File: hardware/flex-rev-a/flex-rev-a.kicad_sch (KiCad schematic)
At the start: 0 parts

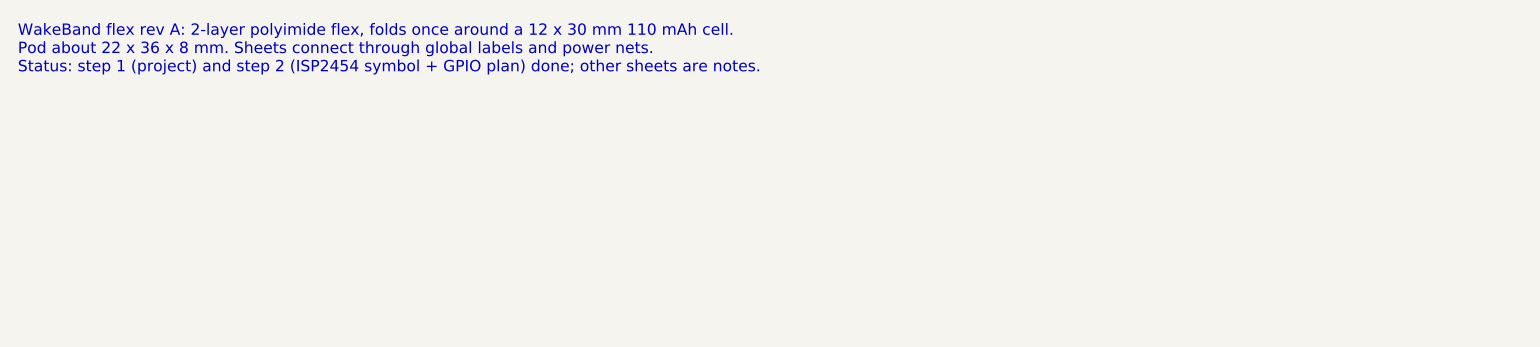
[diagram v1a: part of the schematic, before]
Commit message: Draw nPM1304 power sheet and move the project to KiCad 10 format
Power sheet (step 3 of the flex plan), from Nordic's nPM1304 datasheet
reference circuit "configuration 2" (QFN32):
- VBUS from dock VIN with a TVS and 1 uF; CC1/CC2 to GND (no USB-C).
- VBAT to the cell pads through a cut-able current-measure jumper (JP201).
- BUCK1 at 1.8 V (VSET1 47k, confirmed in the datasheet table) on VDD_1V8,
  2.2 uH + 10 uF; VDDIO from VOUT1; PVSS1 to GND through a net tie.
- BUCK2 unused: VOUT2 to VSYS, VSET2 and PVSS2 to GND, SW2 open, no inductor.
  Load switches unused (pins to GND), LED pins open.
- 10k B3380 NTC, SHPHLD test pad + DNP pull-up and button footprint,
  PMIC_INT on GPIO3, 4.7k I2C pull-ups for the shared 1.8 V bus.
- Temporary PWR_FLAGs on VDD_1V8 and VSYS removed (now driven by the PMIC);
  flags remain only on off-board sources (VIN, cell VBAT/GND) and PVSS1.
- Open items marked (check) on the sheet.

Also: nPM1304-QEAA symbol added to wakeband.kicad_sym, all sheets and the
library saved in KiCad 10 format, PDF replotted, README ERC status, plan
notes updated with datasheet facts (TWI 0x6B, VBUS exits ship mode).

ERC (KiCad 10.0.5): 2 errors, 10 warnings, none on the power sheet; all
wait for the dock/sensors/haptics/debug sheets.

Co-Authored-By: Claude Opus 5.5 <noreply@anthropic.com>
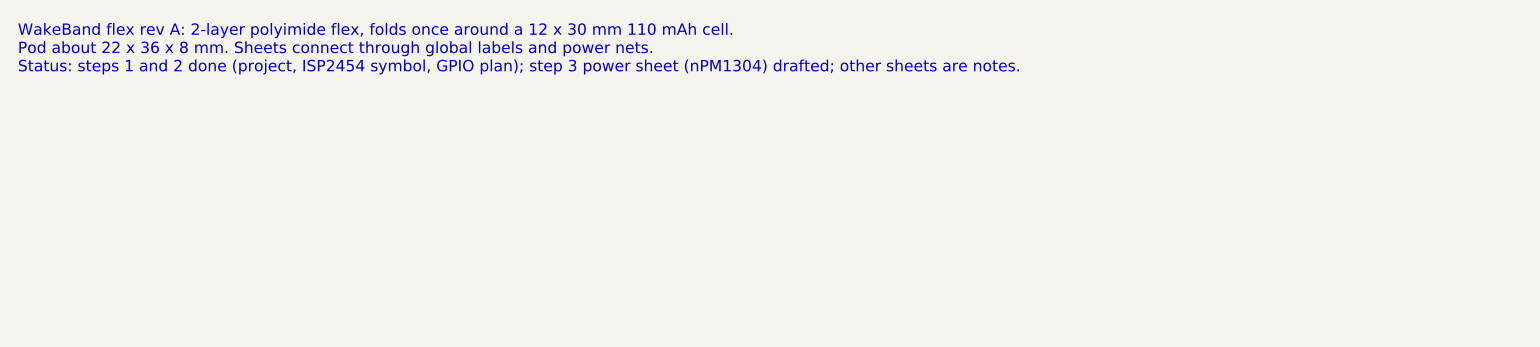
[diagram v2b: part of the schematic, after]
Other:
- note added: "WakeBand flex rev A: 2-layer polyimide flex, folds once around a 12 x 30 mm 110 mAh cell. Pod about 22 x 36 x 8 mm. Sheets connect through global labels and power nets. Status: steps 1 and 2 done (project, ISP2454 symbol, GPIO plan); step 3 power sheet (nPM1304) drafted; other sheets are notes."
- note removed: "WakeBand flex rev A: 2-layer polyimide flex, folds once around a 12 x 30 mm 110 mAh cell. Pod about 22 x 36 x 8 mm. Sheets connect through global labels and power nets. Status: step 1 (project) and step 2 (ISP2454 symbol + GPIO plan) done; other sheets are notes."

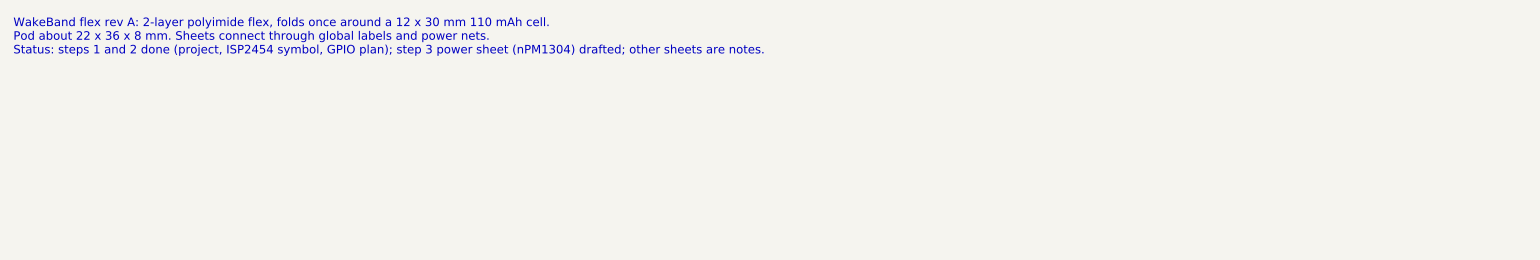
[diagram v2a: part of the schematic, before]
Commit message: Finish rev A schematic pass: clean ERC, BOM with LCSC numbers
- ERC 0 errors, 0 warnings: the ISP2454 symbol's ground pins renamed from
  VSS to GND (same pins), so they no longer clash with the GND label.
- Sensors: larger LIS2DW12 symbol so pin names and GND symbols no longer
  overlap. Dock: connector mirrored and TVS spacing widened for
  readability. No connectivity changes.
- bom.csv: JLCPCB-style columns with LCSC numbers checked on lcsc.com;
  ISP2454-LX and nPM1304-QEAA have none. Pads, jumper and net tie excluded.
- All 50 references annotated and unique; PDF replotted; README status
  table, ERC notes and plan progress updated.

Co-Authored-By: Claude Opus 5.5 <noreply@anthropic.com>
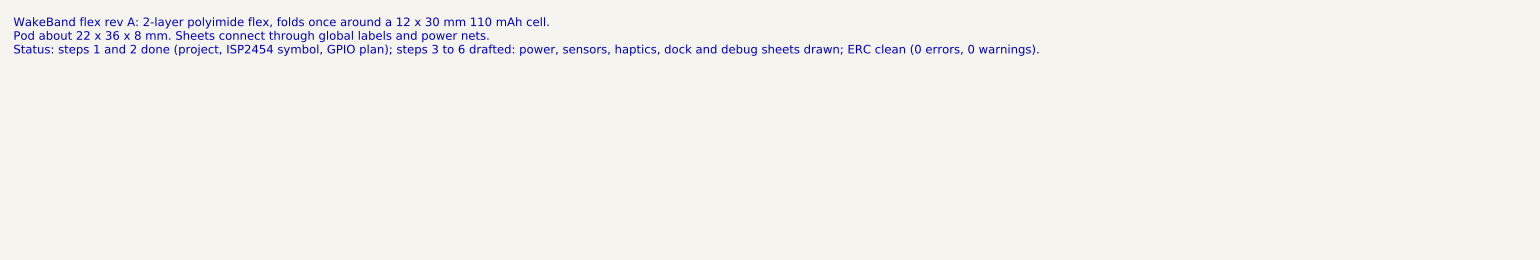
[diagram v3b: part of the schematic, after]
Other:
- note added: "WakeBand flex rev A: 2-layer polyimide flex, folds once around a 12 x 30 mm 110 mAh cell. Pod about 22 x 36 x 8 mm. Sheets connect through global labels and power nets. Status: steps 1 and 2 done (project, ISP2454 symbol, GPIO plan); steps 3 to 6 drafted: power, sensors, haptics, dock and debug sheets drawn; ERC clean (0 errors, 0 warnings)."
- note removed: "WakeBand flex rev A: 2-layer polyimide flex, folds once around a 12 x 30 mm 110 mAh cell. Pod about 22 x 36 x 8 mm. Sheets connect through global labels and power nets. Status: steps 1 and 2 done (project, ISP2454 symbol, GPIO plan); step 3 power sheet (nPM1304) drafted; other sheets are notes."
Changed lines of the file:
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@@
 		)
 	)
-	(text "WakeBand flex rev A: 2-layer polyimide flex, folds once around a 12 x 30 mm 110 mAh cell.\nPod about 22 x 36 x 8 mm. Sheets connect through global labels and power nets.\nStatus: steps 1 and 2 done (project, ISP2454 symbol, GPIO plan); step 3 power sheet (nPM1304) drafted; other sheets are notes."
+	(text "WakeBand flex rev A: 2-layer polyimide flex, folds once around a 12 x 30 mm 110 mAh cell.\nPod about 22 x 36 x 8 mm. Sheets connect through global labels and power nets.\nStatus: steps 1 and 2 done (project, ISP2454 symbol, GPIO plan); steps 3 to 6 drafted: power, sensors, haptics, dock and debug sheets drawn; ERC clean (0 errors, 0 warnings)."
 		(exclude_from_sim no)
 		(at 20.32 20.32 0)
